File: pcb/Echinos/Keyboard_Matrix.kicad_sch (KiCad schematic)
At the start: 61 parts, among them J5 Joystick

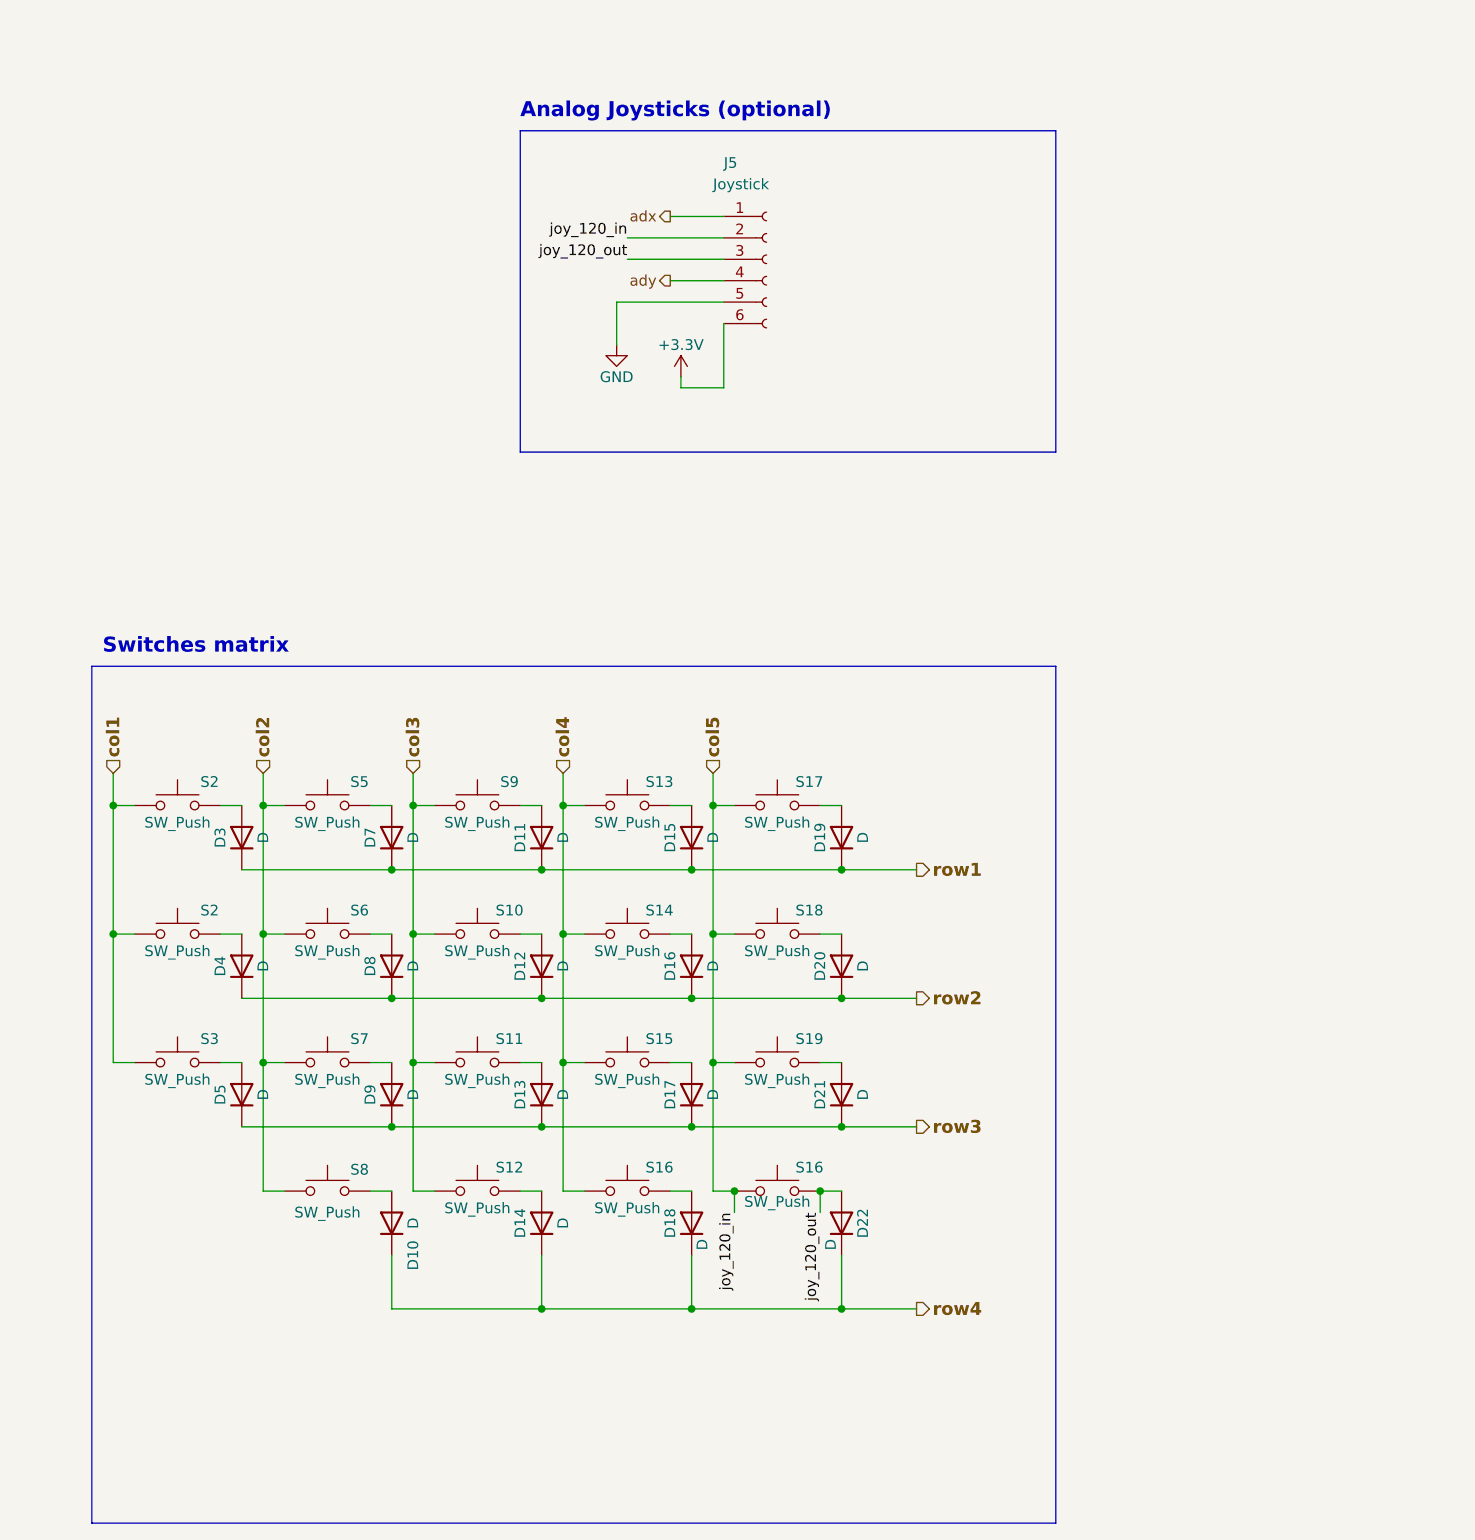
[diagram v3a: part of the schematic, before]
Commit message: [PCB] - Save last state with in-board MCU.
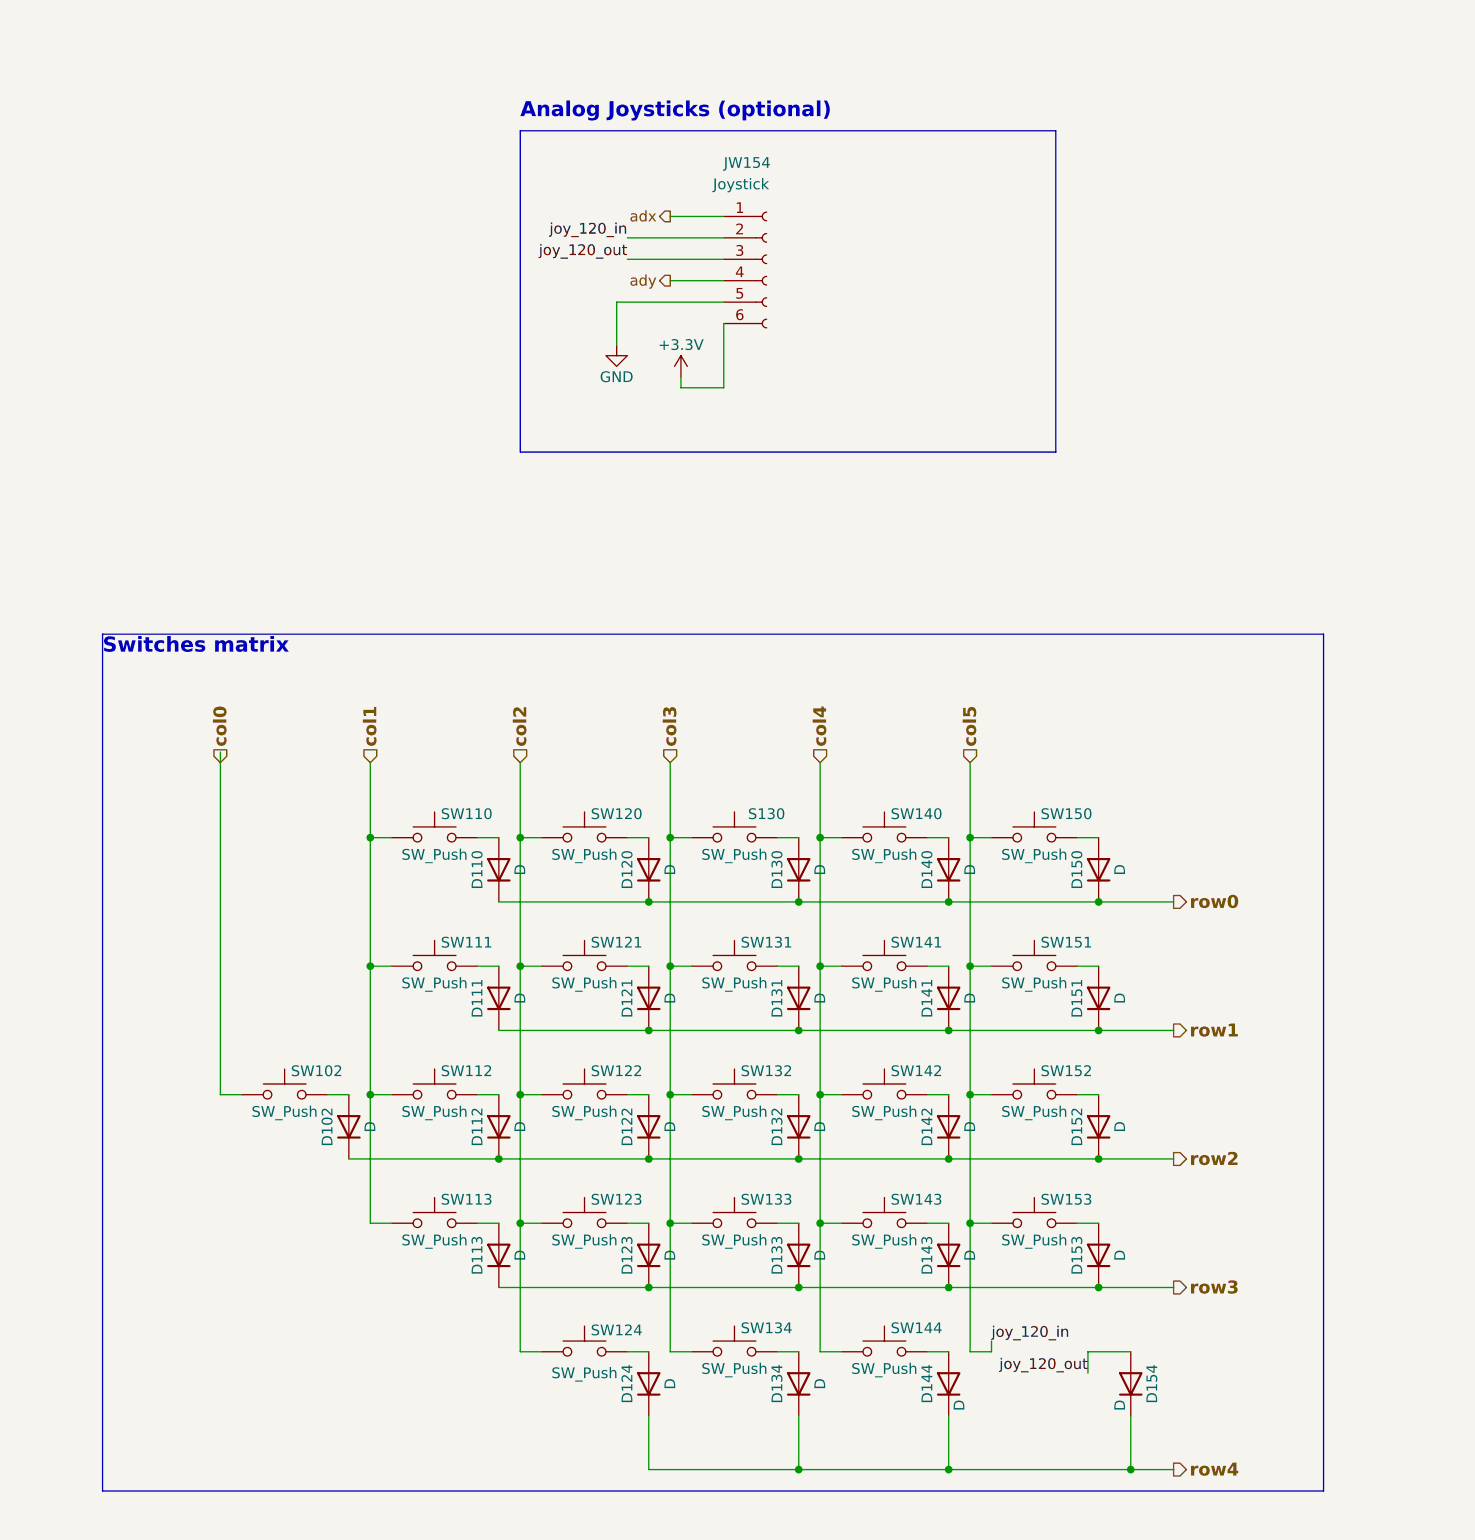
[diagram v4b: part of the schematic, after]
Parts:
- removed S16: SW_Push, Echinos:SW_Choc_MX_KS33_1u_hotswap, symbol Switch:SW_Push
- added D102, D110, D120, D130, D140, D150: D, Echinos:D_SOD123, symbol Device:D
- added S130, SW102, SW110, SW120, SW140, SW150: SW_Push, Echinos:SW_Choc_MX_KS33_1u_hotswap, symbol Switch:SW_Push
- renumbered D3 to D111, D4 to D112, D5 to D113, D7 to D121, D8 to D122, D9 to D123, D10 to D124, D11 to D131, D12 to D132, D13 to D133, D14 to D134, D15 to D141, D16 to D142, D17 to D143, D18 to D144, D19 to D151, D20 to D152, D21 to D153, D22 to D154, J5 to JW154, S2 to SW111, S2 to SW112, S3 to SW113, S5 to SW121, S6 to SW122, S7 to SW123, S8 to SW124, S9 to SW131, S10 to SW132, S11 to SW133, S12 to SW134, S13 to SW141, S14 to SW142, S15 to SW143, S16 to SW144, S17 to SW151, S18 to SW152, S19 to SW153
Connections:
- net col1: now also SW110.1
- net col2: now also SW120.1
- net col3: now also S130.1
- net col4: now also SW140.1
- net col5: now also SW150.1
- net row2: now also D102.1 (K)
- new net: D110.2 (A), SW110.2
- new net: D120.2 (A), SW120.2
- new net: D150.2 (A), SW150.2
- new net: D140.2 (A), SW140.2
- new net: D130.2 (A), S130.2
- new net: D102.2 (A), SW102.2
- new net col0: SW102.1
- new net row0: D110.1 (K), D120.1 (K), D130.1 (K), D140.1 (K), D150.1 (K)
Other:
- moved on the sheet: D111, D112, D113, D121, D122, D123, D124, D131, D132, D133, D134, D141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

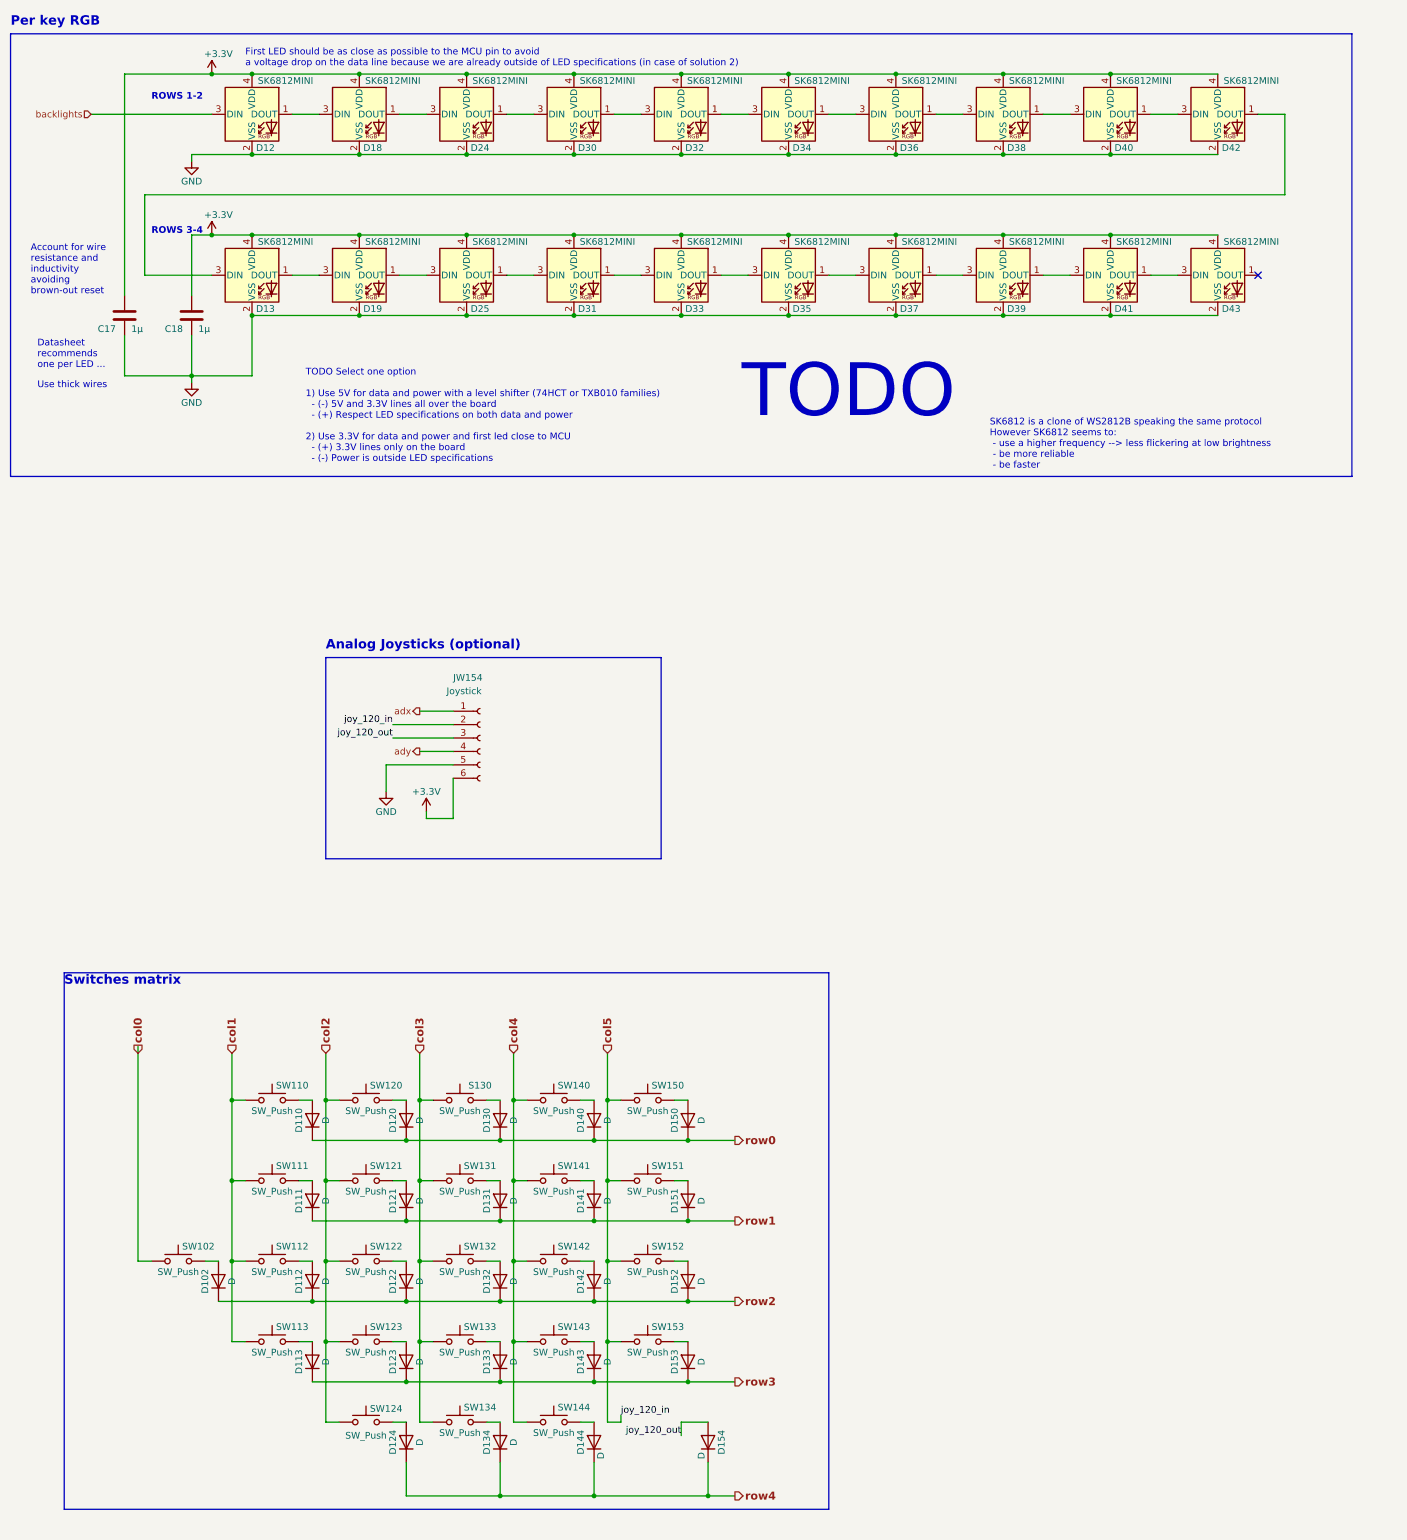
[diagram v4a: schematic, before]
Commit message: [PCB] - Save last state with Gemini MCU board (with mod exposing more pins).
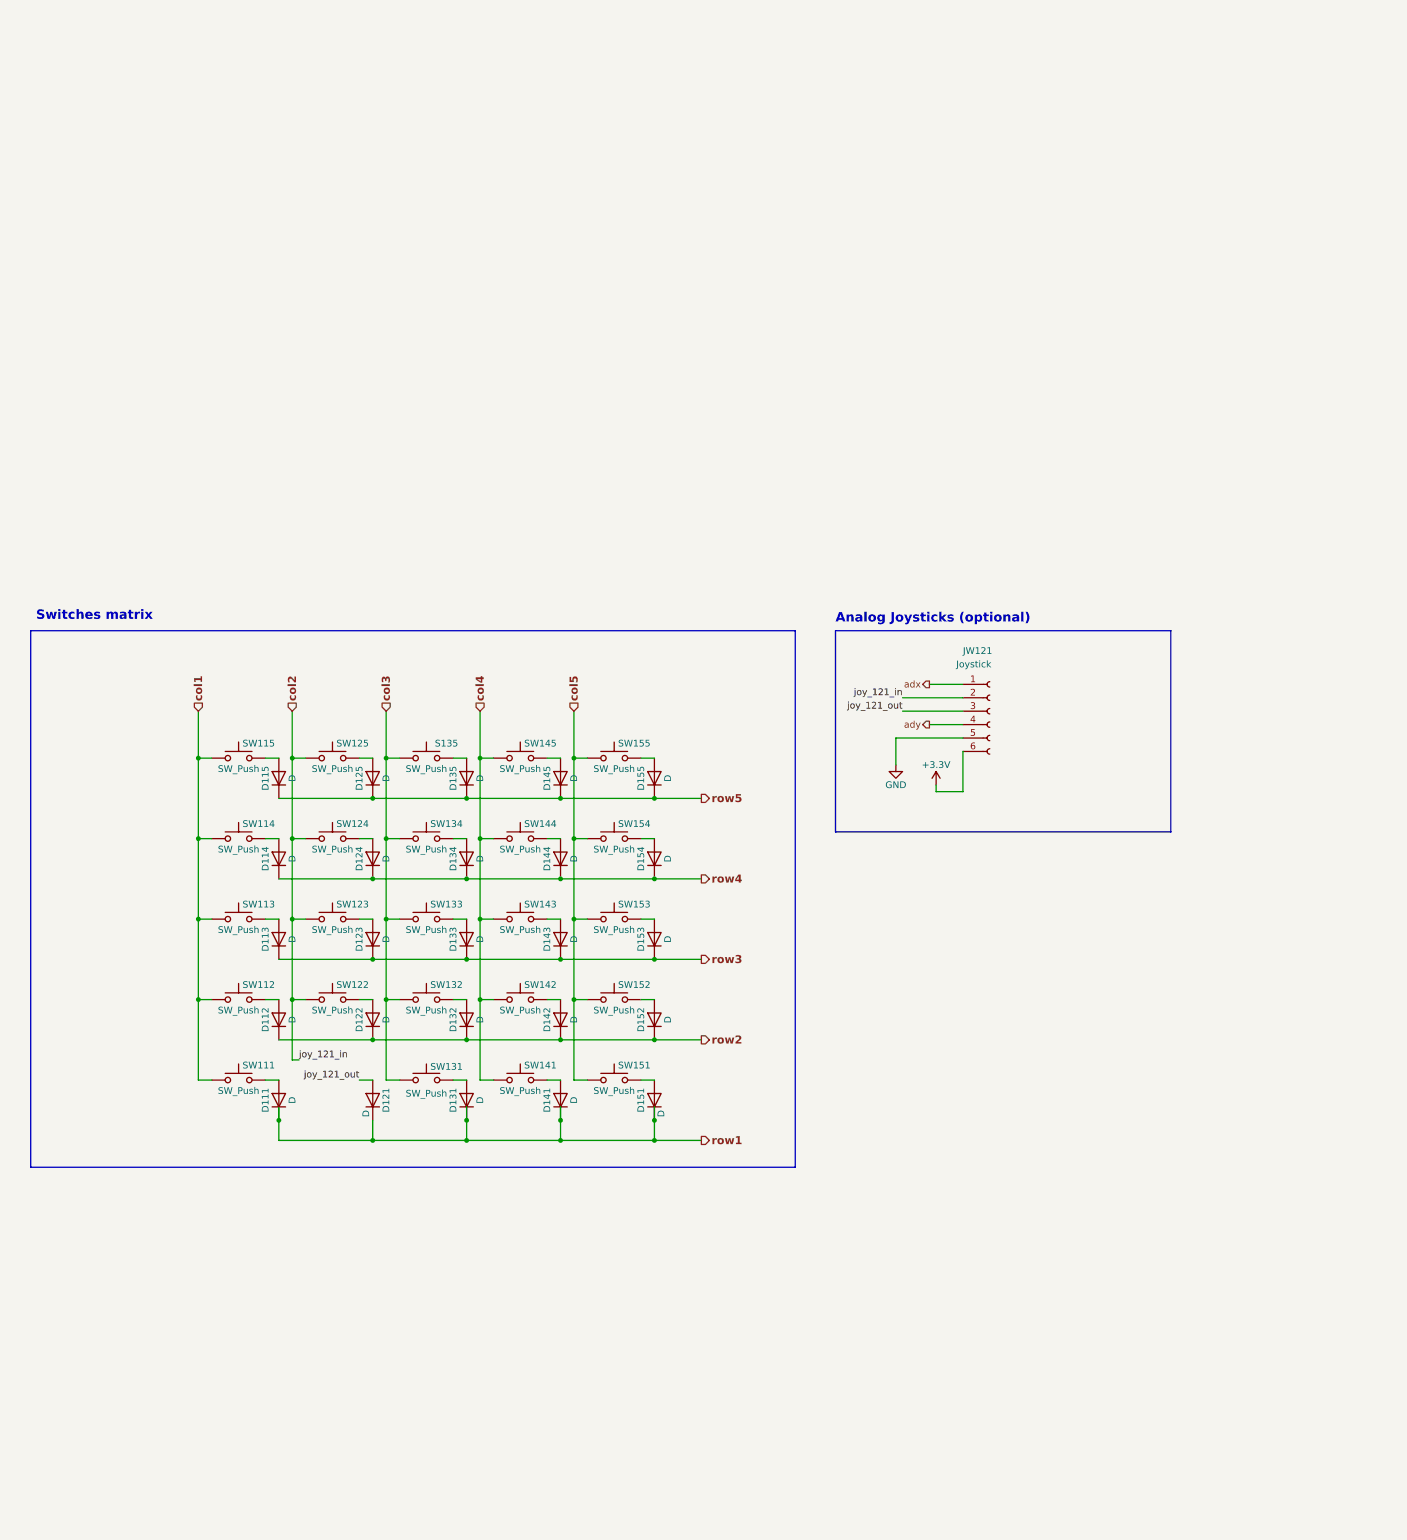
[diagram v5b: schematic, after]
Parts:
- removed C17, C18: 1µ, Capacitor_SMD:C_0402_1005Metric, symbol Device:C
- removed D12, D13, D18, D19, D24, D25, D30, D31, D32, D33, D34, D35, D36, D37, D38, D39, D40, D41, D42, D43: SK6812MINI, LED_SMD:LED_SK6812MINI_PLCC4_3.5x3.5mm_P1.75mm, symbol LED:SK6812MINI
- renumbered D102 to D111, D113 to D112, D112 to D113, D111 to D114, D110 to D115, D154 to D121, D123 to D122, D122 to D123, D121 to D124, D120 to D125, D124 to D131, D133 to D132, D132 to D133, D131 to D134, D130 to D135, D134 to D141, D143 to D142, D142 to D143, D141 to D144, D140 to D145, D144 to D151, D153 to D152, D152 to D153, D151 to D154, D150 to D155, JW154 to JW121, S130 to S135, SW102 to SW111, SW113 to SW112, SW112 to SW113, SW111 to SW114, SW110 to SW115, SW123 to SW122, SW122 to SW123, SW121 to SW124, SW120 to SW125, SW124 to SW131, SW133 to SW132, SW132 to SW133, SW131 to SW134, SW134 to SW141, SW143 to SW142, SW142 to SW143, SW141 to SW144, SW140 to SW145, SW144 to SW151, SW153 to SW152, SW152 to SW153, SW151 to SW154, SW150 to SW155
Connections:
- net col0 is gone; now on net col1: SW111.1
- net col2: now also JW121.2 (Pin_2); no longer SW131.1
- net col3: now also SW131.1; no longer SW141.1
- net col4: now also SW141.1; no longer SW151.1
- net col5: now also SW151.1; no longer JW121.2 (Pin_2)
- net row1: now also D111.1 (K), D121.1 (K), D131.1 (K), D141.1 (K), D151.1 (K); no longer D114.1 (K), D124.1 (K), D134.1 (K), D144.1 (K), D154.1 (K)
- net row2: now also D112.1 (K), D122.1 (K), D132.1 (K), D142.1 (K), D152.1 (K); no longer D111.1 (K), D113.1 (K), D123.1 (K), D133.1 (K), D143.1 (K), D153.1 (K)
- net row3: now also D113.1 (K), D123.1 (K), D133.1 (K), D143.1 (K), D153.1 (K); no longer D112.1 (K), D122.1 (K), D132.1 (K), D142.1 (K), D152.1 (K)
- net row4: now also D114.1 (K), D124.1 (K), D134.1 (K), D144.1 (K), D154.1 (K); no longer D121.1 (K), D131.1 (K), D141.1 (K), D151.1 (K)
- net joy_120_out renamed joy_121_out
- net row0 renamed row5
- no-connect marks 1 -> 0
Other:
- note removed: "Account for wire resistance and inductivity avoiding brown-out reset"
- note removed: "Datasheet recommends one per LED ..."
- note removed: "First LED should be as close as possible to the MCU pin to avoid a voltage drop on the data line because we are already outside of LED specifications (in case of solution 2)"
- note removed: "Per key RGB"
- note removed: "ROWS 1-2"
- note removed: "ROWS 3-4"
- note removed: "SK6812 is a clone of WS2812B speaking the same protocol However SK6812 seems to: - use a higher frequency --> less flickering at low brightness - be more reliable - be faster"
- note removed: "TODO"
- note removed: "TODO Select one option 1) Use 5V for data and power with a level shifter (74HCT or TXB010 families) - (-) 5V and 3.3V lines all over the board - (+) Respect LED specifications on both data and power 2) Use 3.3V for data and power and first led close to MCU - (+) 3.3V lines only on the board - (-) Power is outside LED specifications"
- note removed: "Use thick wires"
- moved on the sheet: D111, D112, D113, D114, D115, D121, D122, D123, D124, D125, D131, D132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
